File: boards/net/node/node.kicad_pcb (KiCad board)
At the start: 4 copper layers, 48 x 48 mm, 60 parts, among them J1 N, J2 E, J3 S, J4 W, J5 SENSOR, J6 PROG, SW1 SW-18010P, U1 RP2040, U2 W25Q16JVSSIQ, U3 VL53L0CXV0DH/1, U4 ME6211C33M5G, Y1 12MHz

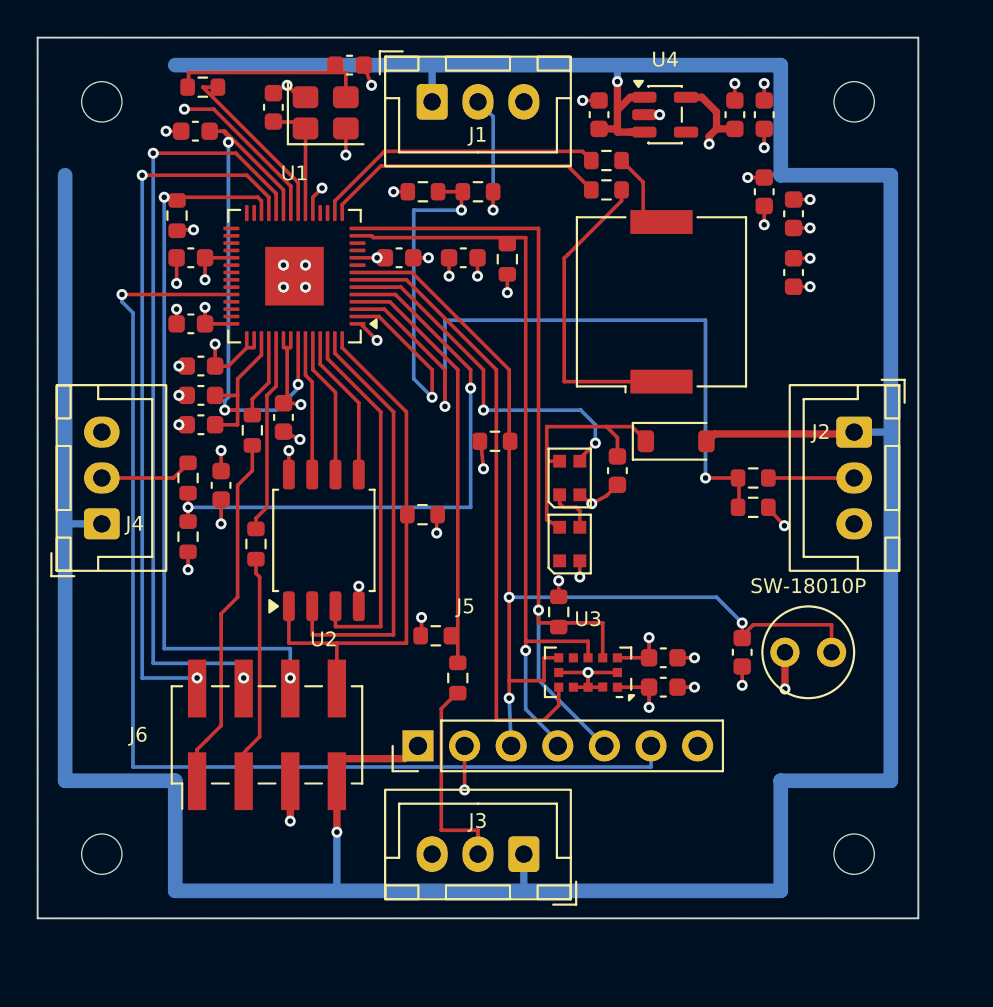
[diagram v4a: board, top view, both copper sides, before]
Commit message: net/node: C11 (1 uF VREG_VIN) back under pin 44; cap column and R13/R14 shifted down (Codex finding 1)
Column at x 8.9 is now C10 17.9 / C11 19.5 / C13 21.1 / C15 22.7; C16, R13/R14, the LINK_W
run (y 26.6) and R3's via moved to suit. make check clean.

Co-Authored-By: Claude Fable 5.1 <noreply@anthropic.com>
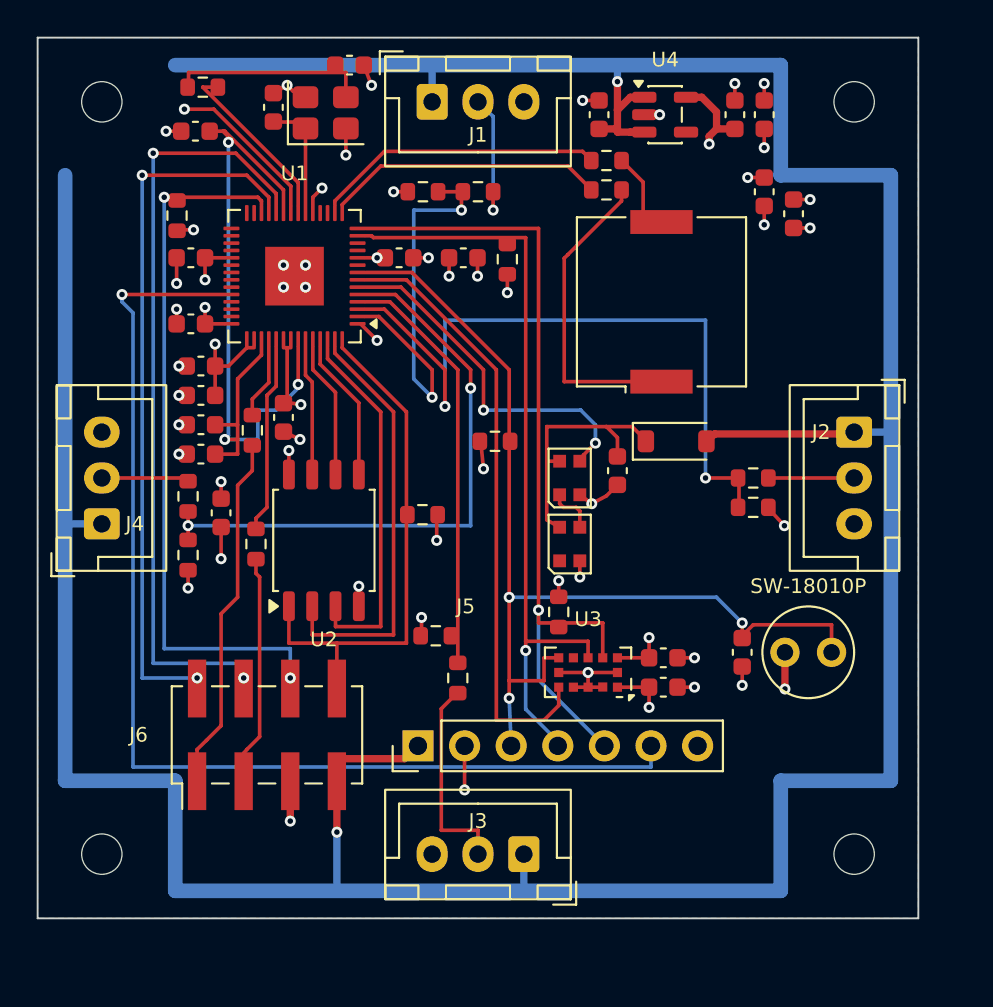
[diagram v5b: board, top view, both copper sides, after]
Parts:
- moved C11 33.0 mm to (58.9, 69.5), turned to 180 degrees
- moved C15 1.60 mm to (58.9, 72.7)
- moved C13 1.60 mm to (58.9, 71.1)
- moved C16 1.50 mm to (60.0, 75.9)
- moved R13 1.00 mm to (58.2, 75.0)
- moved R14 1.00 mm to (58.2, 78.2)
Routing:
- net /DVDD: track 35.3 -> 40.1 mm
- net +3V3: track 51.4 -> 52.8 mm, vias 27 -> 26
- net /LINK_W: track 32.0 -> 32.9 mm
- net GND: track 37.6 -> 36.9 mm

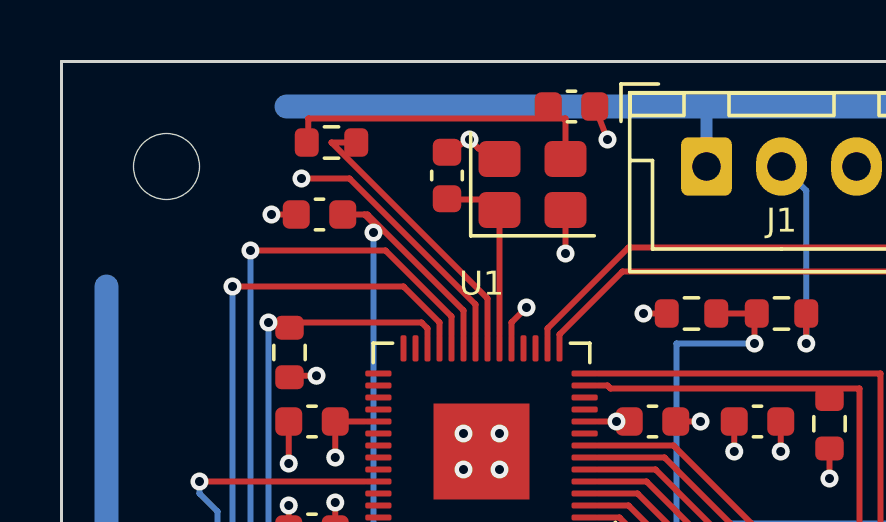
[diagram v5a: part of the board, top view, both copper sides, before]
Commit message: net/node: tighter crystal loop (Codex finding 2): R1 on the XOUT row end, Y1 rotated beside it, node along the top
Loop 20 -> ~17 mm; the remaining 8.8 mm XOUT diagonal is the fan itself. make check clean.

Co-Authored-By: Claude Fable 5.1 <noreply@anthropic.com>
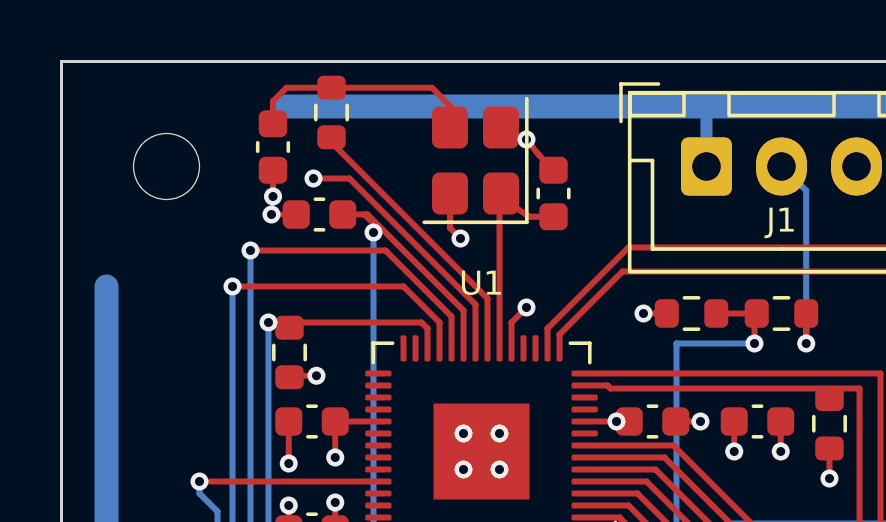
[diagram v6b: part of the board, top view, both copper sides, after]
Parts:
- moved C2 10.0 mm to (57.0, 52.9), turned to 90 degrees
- moved C1 3.60 mm to (66.4, 54.4)
- moved Y1 2.06 mm to (63.8, 53.3), turned to 90 degrees
- moved R1 1.00 mm to (59.0, 51.7), turned to -90 degrees
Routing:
- net Net-(C2-Pad2): track 10.7 -> 7.81 mm
- net Net-(U1-XIN): track 4.15 -> 6.76 mm
- net Net-(U1-XOUT): track 9.35 -> 8.75 mm

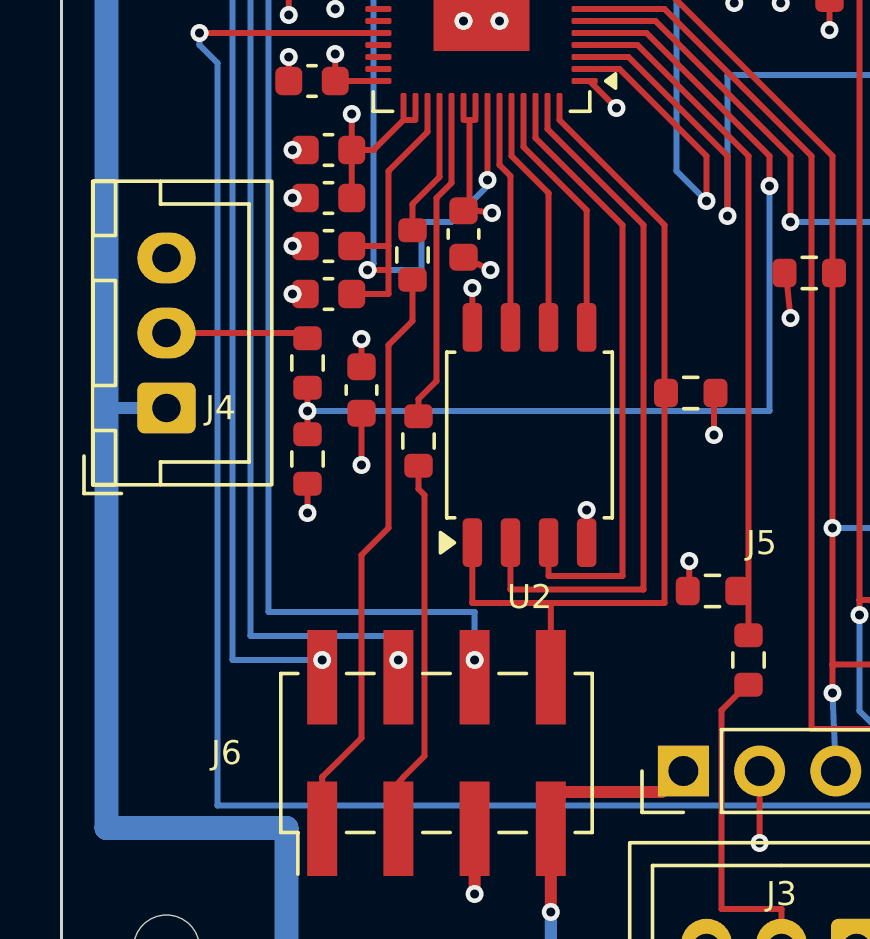
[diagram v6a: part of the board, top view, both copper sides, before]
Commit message: net/node: USB series resistors stacked under the pins, DM/DP run as a pair (Codex finding 3)
R15 at 4 mm, R16 at 7 mm from U1 (one 0603 column fits between the DVDD track and U2);
DP/DM 0.8 mm apart down to J6. make check clean.

Co-Authored-By: Claude Fable 5.1 <noreply@anthropic.com>
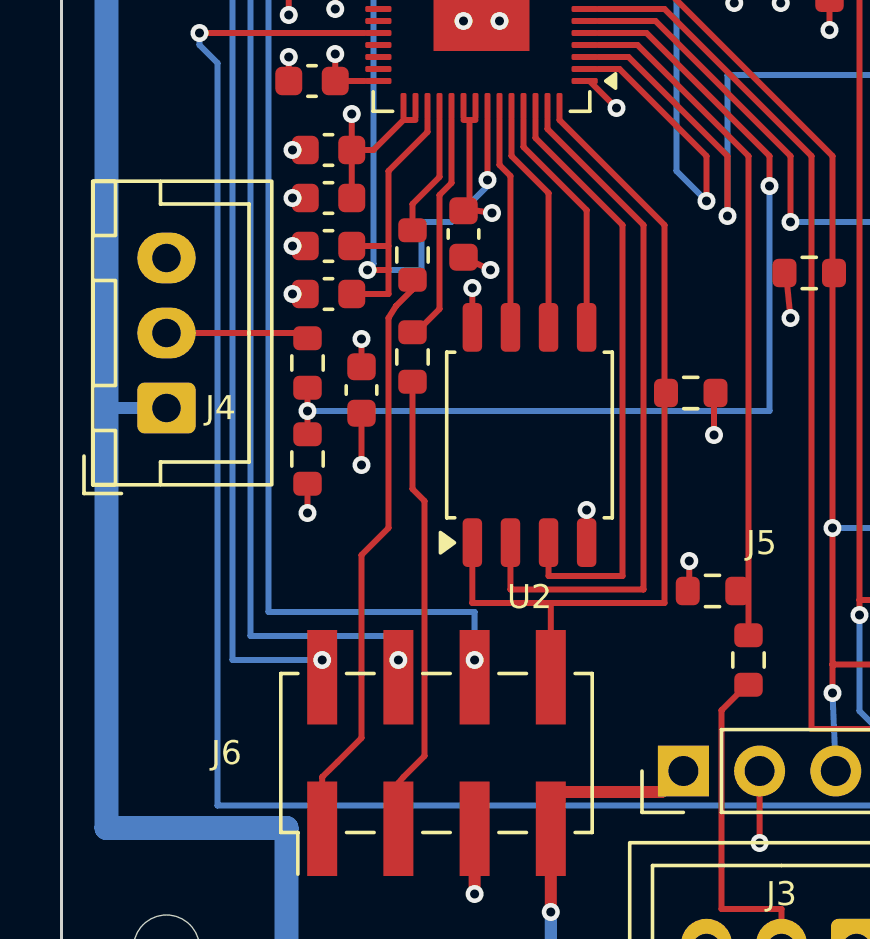
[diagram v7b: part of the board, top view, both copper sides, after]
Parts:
- moved R16 2.81 mm to (61.7, 74.8)
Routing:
- net Net-(J6-Pin_3): track 12.6 -> 15.4 mm
- net /USB_DP: track 10.4 -> 7.69 mm

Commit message: net/node: pogo pads without paste apertures (Codex finding 4); pcbgen no_paste option
J6 now uses boards:PogoPads_2x04_P2.54mm (stock 2x4 SMD header minus F.Paste, no 3D model)
so DRC does not flag a library mismatch; the F.Paste gerber no longer contains J6.
pcbgen.footprint(no_paste=True) strips paste layers for the same purpose on stock
footprints (tested). make test, make check clean.

Co-Authored-By: Claude Fable 5.1 <noreply@anthropic.com>
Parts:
- J6: footprint Connector_PinHeader_2.54mm:PinHeader_2x04_P2.54mm_Vertical_SMD -> boards:PogoPads_2x04_P2.54mm
